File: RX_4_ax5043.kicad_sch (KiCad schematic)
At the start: 22 parts, among them P23 CONUFL001-SMD-T, P4 CONUFL001-SMD-T, Q6 DMP2160UWQ-7, U19 AX5043

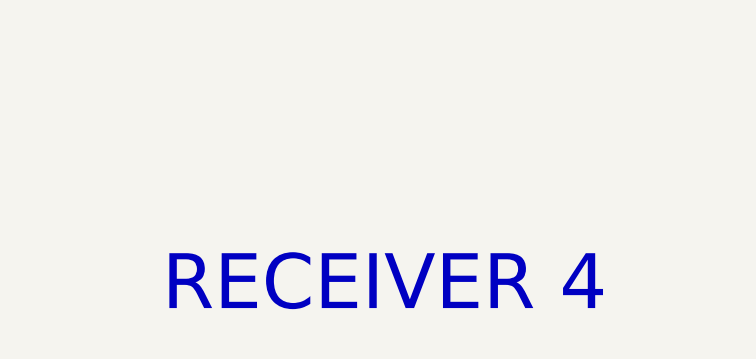
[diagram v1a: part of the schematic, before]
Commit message: Add licensing
Use CERN-OHL-W version 2

Signed-off-by: Corey Minyard <corey@minyard.net>
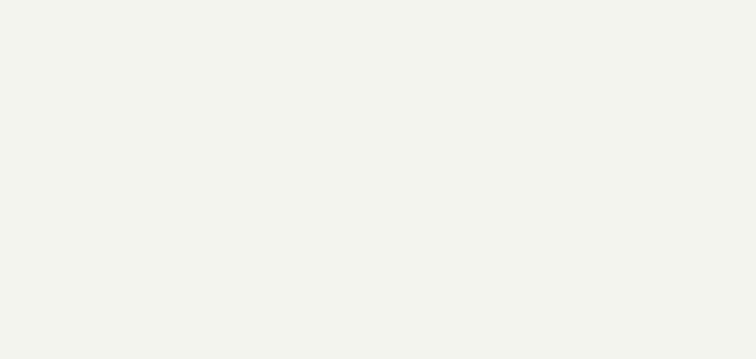
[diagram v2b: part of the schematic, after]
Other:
- note removed: "RECEIVER 4"
- title: Radiation Tolerant PacSat Communication -> AX5043 Receiver 1
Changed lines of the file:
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@@
 	(paper "USLedger")
 	(title_block
-		(title "Radiation Tolerant PacSat Communication")
-		(date "2023-06-17")
-		(rev "A")
+		(title "AX5043 Receiver 1")
+		(date "2026-08-20")
+		(rev "4.0")
 		(company "AMSAT-NA")
-		(comment 1 "N5BRG")
+		(comment 1 "AE5KM")
+		(comment 2 "Copyright Corey Minyard, 2026")
+		(comment 3 "Licensed under CERN-OHL-W version 2")
 	)
 	(text "Matching circuit for bringing\nTX from the AX5043 off the board."
@@
 		)
 	)
-	(text "RECEIVER 4"
-		(exclude_from_sim no)
-		(at 341.63 247.65 0)
-		(effects
-			(font
-				(size 6.096 6.096)
-			)
-			(justify left bottom)
-		)
-	)

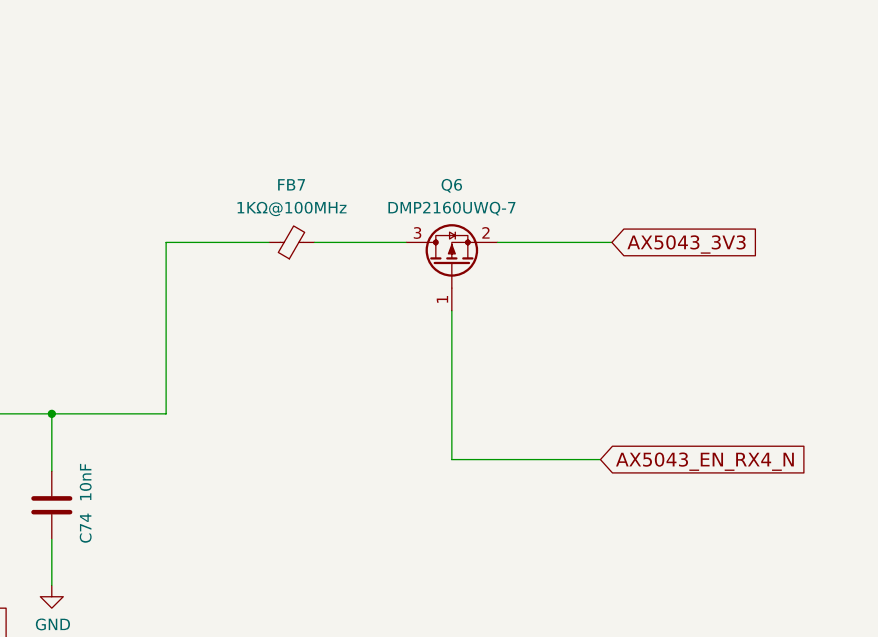
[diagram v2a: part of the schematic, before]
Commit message: Cost reduce the AX5043 power control
Change the MOSFET + ferrite bead combo on all the AX5043 power inputs
to a inrush-controlled power controller.  The space-rated ferrites are
just too expensive.

Signed-off-by: Corey Minyard <corey@minyard.net>
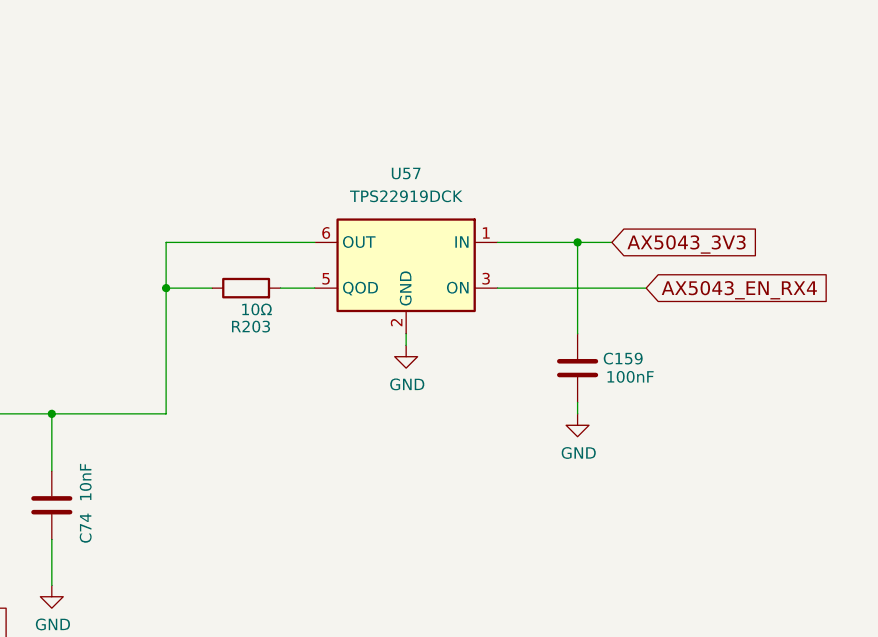
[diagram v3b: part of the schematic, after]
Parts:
- removed FB7: 1KΩ@100MHz, Inductor_SMD:L_0603_1608Metric_Pad1.05x0.95mm_HandSolder, symbol Device:FerriteBead_Small
- removed Q6: DMP2160UWQ-7, Package_TO_SOT_SMD:SOT-323_SC-70, symbol Transistor_FET:Q_PMOS_GSD
- added C159: 100nF, Capacitor_SMD:C_0402_1005Metric_Pad0.74x0.62mm_HandSolder, symbol Device:C
- added R203: 10Ω, Resistor_SMD:R_0402_1005Metric_Pad0.72x0.64mm_HandSolder, symbol Device:R
- added U57: TPS22919DCK, Package_TO_SOT_SMD:SOT-363_SC-70-6, symbol Power_Management:TPS22919DCK
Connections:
- net AX5043_3V3: now also C159.1, U57.1 (IN)
- net GND: now also C159.2, U57.2 (GND)
- net at C74.1, U19.23 (VDD_IO): now also R203.1, U57.6 (OUT)
- new net: R203.2, U57.5 (QOD)
- new net AX5043_EN_RX4: U57.3 (ON)

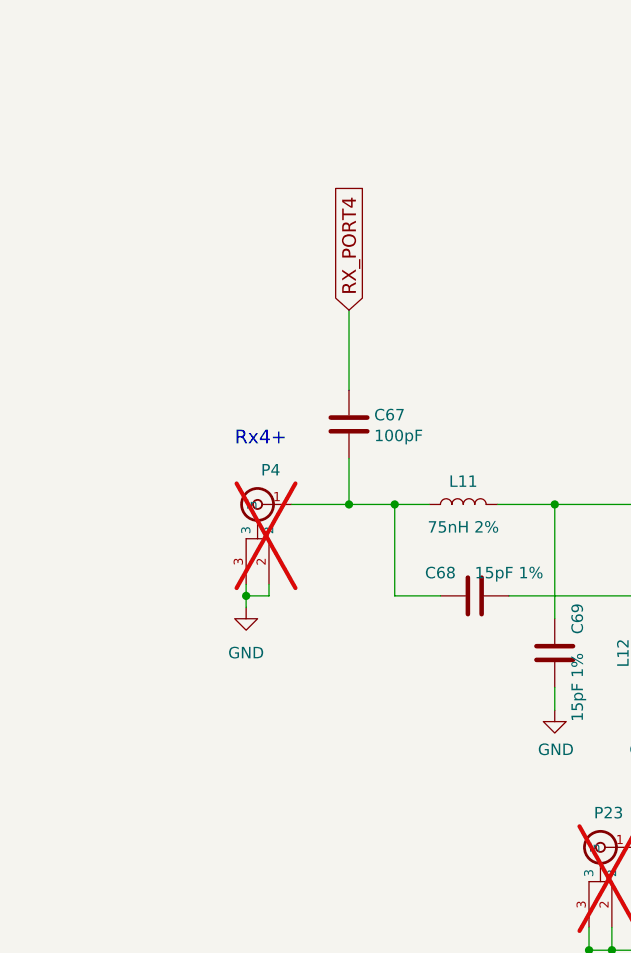
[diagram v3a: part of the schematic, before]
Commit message: Remove U.FL connectors from all AX5043 RX connections except AX5043 4
They aren't necessary.  If you need to pull off an RX line for another
board, you can use 4, and you can use 4 for testing.

Signed-off-by: Corey Minyard <corey@minyard.net>
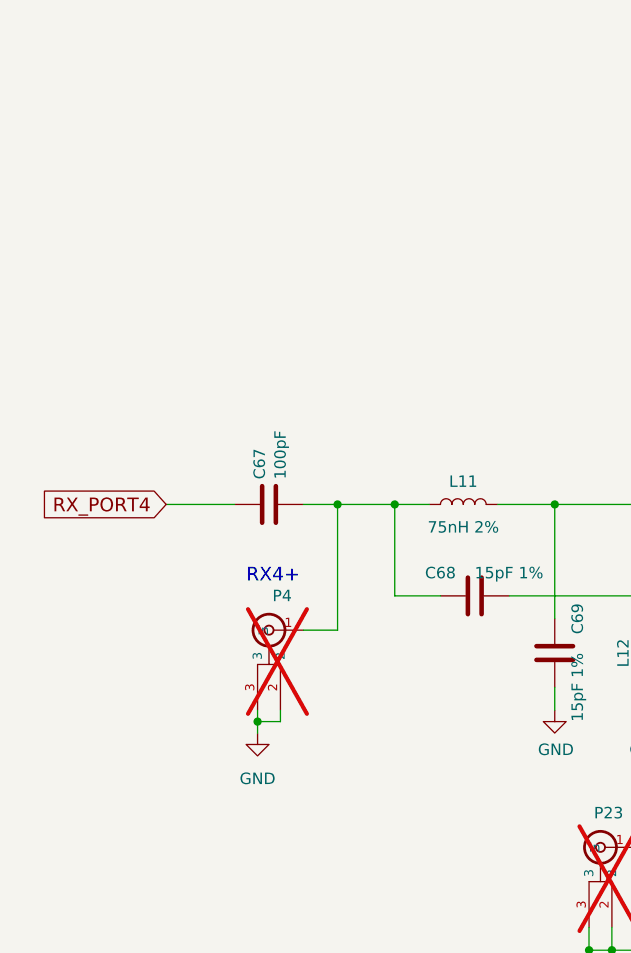
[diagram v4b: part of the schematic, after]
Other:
- note added: "RX4+"
- note removed: "Rx4+"
- moved on the sheet: C67
